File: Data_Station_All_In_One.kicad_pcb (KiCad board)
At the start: 2 copper layers, 97.8 x 76.2 mm, 55 parts, among them J1 Conn_01x02_Male, J10 Conn_01x02_Male, J11 USB_B_Micro, J12 Conn_01x02_Male, J2 Conn_01x02_Male, J3 Conn_01x02_Male, J4 Conn_01x02_Male, J5 Conn_01x02_Male, J6 Conn_01x02_Male, J7 Conn_01x06_Male, J8 Conn_01x06_Male, J9 Conn_01x03_Male, Q1 2N2222, Q2 2N2222, U1 LM7805_TO220, U2 ATMEGA328P-PU, U3 FT232RL, Y1 Crystal

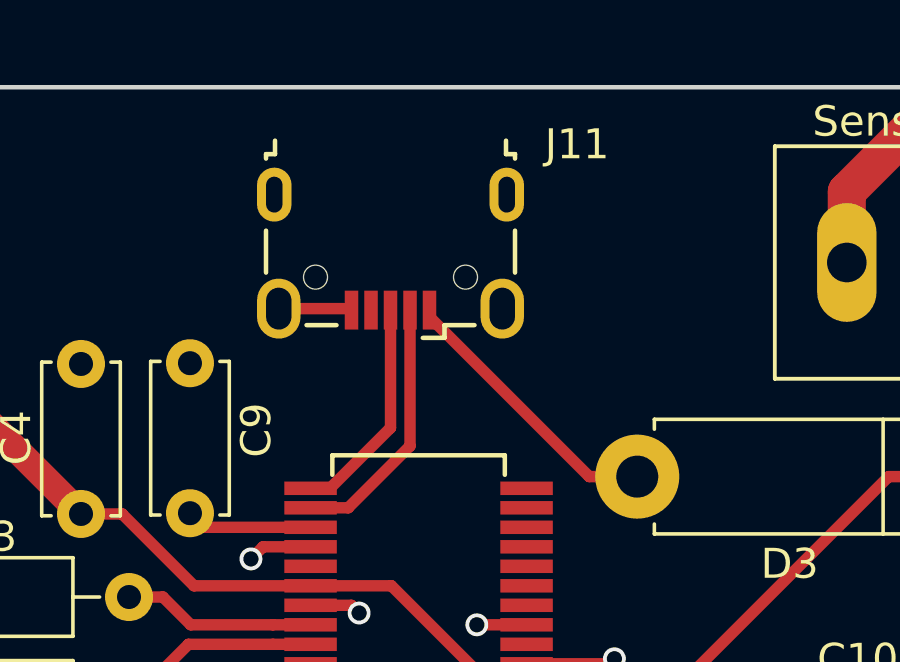
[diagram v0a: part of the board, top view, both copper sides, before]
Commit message: Moved USB Micro to PCB Edge
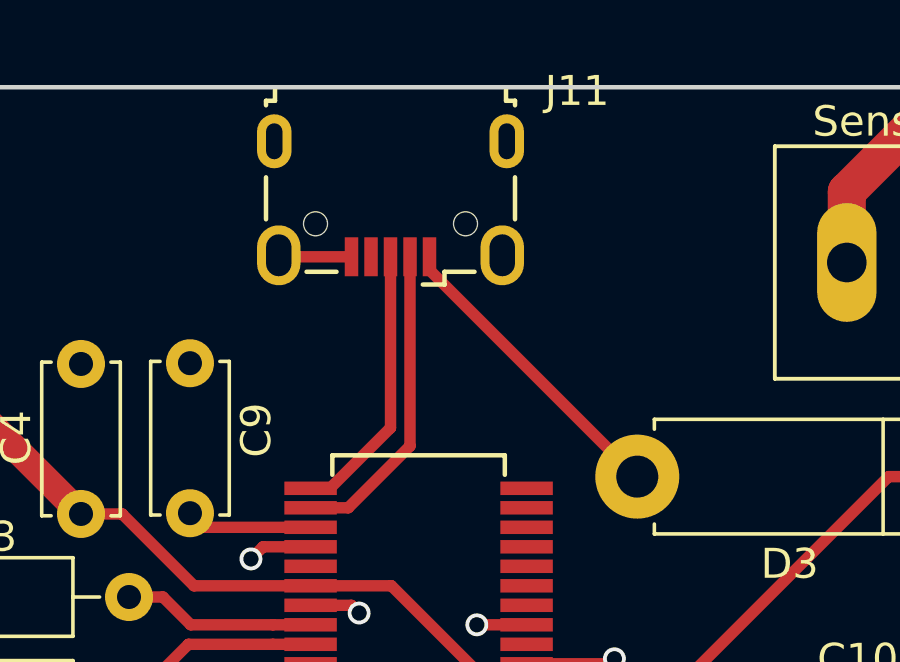
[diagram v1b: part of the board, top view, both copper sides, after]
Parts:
- moved J11 1.78 mm to (126.4, 54.6)
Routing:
- net Net-(J11-Pad3): track 7.42 -> 9.20 mm
- net Net-(J11-Pad2): track 8.70 -> 10.5 mm
- net Net-(D3-Pad2): track 9.36 -> 10.2 mm
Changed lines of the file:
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@@
   )
   (module Connectors_USB:USB_Micro-B_Wuerth-629105150521 (layer F.Cu)
-    (at 126.395 56.3295 180)
+    (at 126.395 54.5515 180)
     (descr "USB Micro-B receptacle, http://www.mouser.com/ds/2/445/629105150521-469306.pdf")
     (tags "usb micro receptacle")
@@
   (segment (start 130.9302 68.7186) (end 129.2722 68.7186) (width 0.381) (layer F.Cu) (net 2) (status 10))
   (via (at 129.2722 68.7186) (size 0.762) (drill 0.508) (layers F.Cu B.Cu) (net 2))
-  (segment (start 125.045 58.1795) (end 125.095 58.2295) (width 0.381) (layer F.Cu) (net 2) (status 30))
-  (segment (start 122.67 58.1795) (end 125.045 58.1795) (width 0.381) (layer F.Cu) (net 2) (status 30))
   (segment (start 181.509 111.786) (end 181.483 111.76) (width 0.381) (layer F.Cu) (net 2) (status 30))
   (segment (start 181.509 115.443) (end 181.509 111.786) (width 0.889) (layer F.Cu) (net 2) (status 30))
@@
   (via (at 125.349 68.326) (size 0.762) (drill 0.508) (layers F.Cu B.Cu) (net 2))
   (segment (start 123.7302 68.0686) (end 125.0916 68.0686) (width 0.381) (layer F.Cu) (net 2) (status 10))
+  (segment (start 122.72 56.4515) (end 122.67 56.4015) (width 0.381) (layer F.Cu) (net 2))
+  (segment (start 125.095 56.4515) (end 122.72 56.4515) (width 0.381) (layer F.Cu) (net 2))
   (segment (start 144.526 98.044) (end 147.066 98.044) (width 1.27) (layer F.Cu) (net 3) (status 20))
   (segment (start 139.446 92.964) (end 144.526 98.044) (width 1.27) (layer F.Cu) (net 3) (status 10))
@@
   (segment (start 188.261 56.642) (end 186.89 56.642) (width 0.762) (layer F.Cu) (net 13) (status 10))
   (segment (start 186.89 56.642) (end 166.624 76.908) (width 0.762) (layer F.Cu) (net 13))
-  (segment (start 193.04 68.58) (end 199.39 68.58) (width 0.381) (layer F.Cu) (net 39) (status 30))
   (segment (start 163.322 81.3435) (end 163.322 80.264) (width 0.381) (layer F.Cu) (net 14) (status 20))
   (segment (start 159.7025 84.963) (end 163.322 81.3435) (width 0.381) (layer F.Cu) (net 14))
@@
   (segment (start 162.052 108.331) (end 163.31037 108.331) (width 0.381) (layer F.Cu) (net 25) (status 10))
   (segment (start 163.31037 108.331) (end 164.45337 109.474) (width 0.381) (layer F.Cu) (net 25))
-  (segment (start 126.395 58.2295) (end 126.395 62.1538) (width 0.381) (layer F.Cu) (net 40) (status 10))
-  (segment (start 124.3802 64.1686) (end 123.7302 64.1686) (width 0.381) (layer F.Cu) (net 40) (status 30))
-  (segment (start 126.395 62.1538) (end 124.3802 64.1686) (width 0.381) (layer F.Cu) (net 40) (status 20))
-  (segment (start 124.9862 64.8186) (end 123.7302 64.8186) (width 0.381) (layer F.Cu) (net 41) (status 20))
-  (segment (start 127.045 58.2295) (end 127.045 62.7598) (width 0.381) (layer F.Cu) (net 41) (status 10))
-  (segment (start 127.045 62.7598) (end 124.9862 64.8186) (width 0.381) (layer F.Cu) (net 41))
   (segment (start 147.066 108.204) (end 151.892 108.204) (width 0.381) (layer F.Cu) (net 26) (status 30))
   (segment (start 151.892 105.156) (end 151.892 108.204) (width 0.381) (layer F.Cu) (net 26) (status 30))
@@
   (segment (start 162.052 105.029) (end 163.449 105.029) (width 0.381) (layer F.Cu) (net 36) (status 10))
   (segment (start 163.449 105.029) (end 164.592 103.886) (width 0.381) (layer F.Cu) (net 36))
-  (segment (start 133.0198 63.7794) (end 134.62 63.7794) (width 0.381) (layer F.Cu) (net 37) (status 20))
-  (segment (start 127.695 58.2295) (end 127.695 58.4546) (width 0.381) (layer F.Cu) (net 37) (status 30))
-  (segment (start 127.695 58.4546) (end 133.0198 63.7794) (width 0.381) (layer F.Cu) (net 37) (status 10))
+  (segment (start 134.5819 63.7794) (end 134.62 63.7794) (width 0.381) (layer F.Cu) (net 37))
+  (segment (start 127.695 56.4515) (end 127.695 56.8925) (width 0.381) (layer F.Cu) (net 37))
+  (segment (start 127.695 56.8925) (end 134.5819 63.7794) (width 0.381) (layer F.Cu) (net 37))
   (segment (start 199.263 76.073) (end 199.39 76.2) (width 0.381) (layer F.Cu) (net 38) (status 30))
   (segment (start 192.405 76.073) (end 199.263 76.073) (width 0.381) (layer F.Cu) (net 38) (status 20))
   (segment (start 185.801 73.533) (end 189.865 73.533) (width 0.381) (layer F.Cu) (net 38) (status 10))
   (segment (start 189.865 73.533) (end 192.405 76.073) (width 0.381) (layer F.Cu) (net 38))
+  (segment (start 193.04 68.58) (end 199.39 68.58) (width 0.381) (layer F.Cu) (net 39) (status 30))
+  (segment (start 124.3802 64.1686) (end 123.7302 64.1686) (width 0.381) (layer F.Cu) (net 40))
+  (segment (start 126.395 56.4515) (end 126.395 62.1538) (width 0.381) (layer F.Cu) (net 40))
+  (segment (start 126.395 62.1538) (end 124.3802 64.1686) (width 0.381) (layer F.Cu) (net 40))
+  (segment (start 124.9862 64.8186) (end 123.7302 64.8186) (width 0.381) (layer F.Cu) (net 41))
+  (segment (start 127.045 56.4515) (end 127.045 62.7598) (width 0.381) (layer F.Cu) (net 41))
+  (segment (start 127.045 62.7598) (end 124.9862 64.8186) (width 0.381) (layer F.Cu) (net 41))
   (segment (start 175.316 118.943) (end 175.26 118.999) (width 0.381) (layer F.Cu) (net 42) (status 30))
   (segment (start 175.26 118.999) (end 169.799 118.999) (width 0.889) (layer F.Cu) (net 42) (status 30))

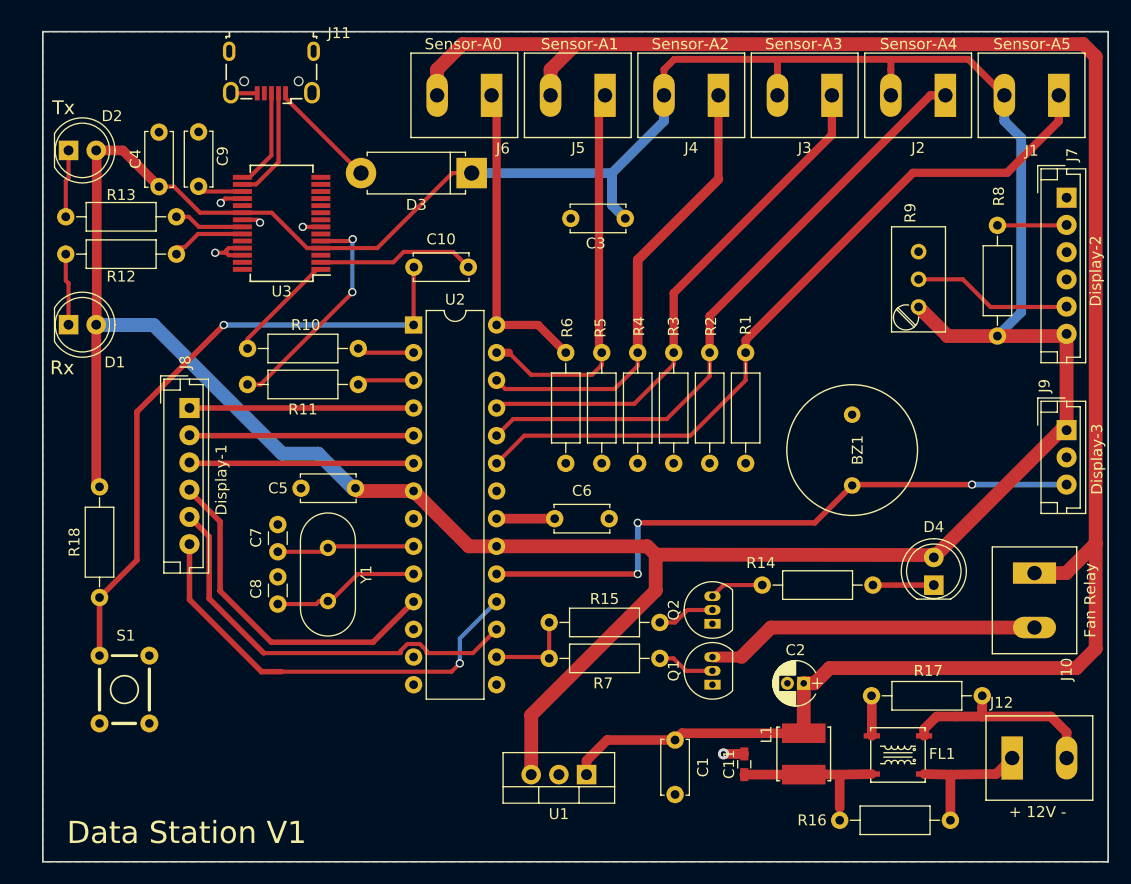
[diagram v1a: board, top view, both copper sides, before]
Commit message: updated to reflect actual order
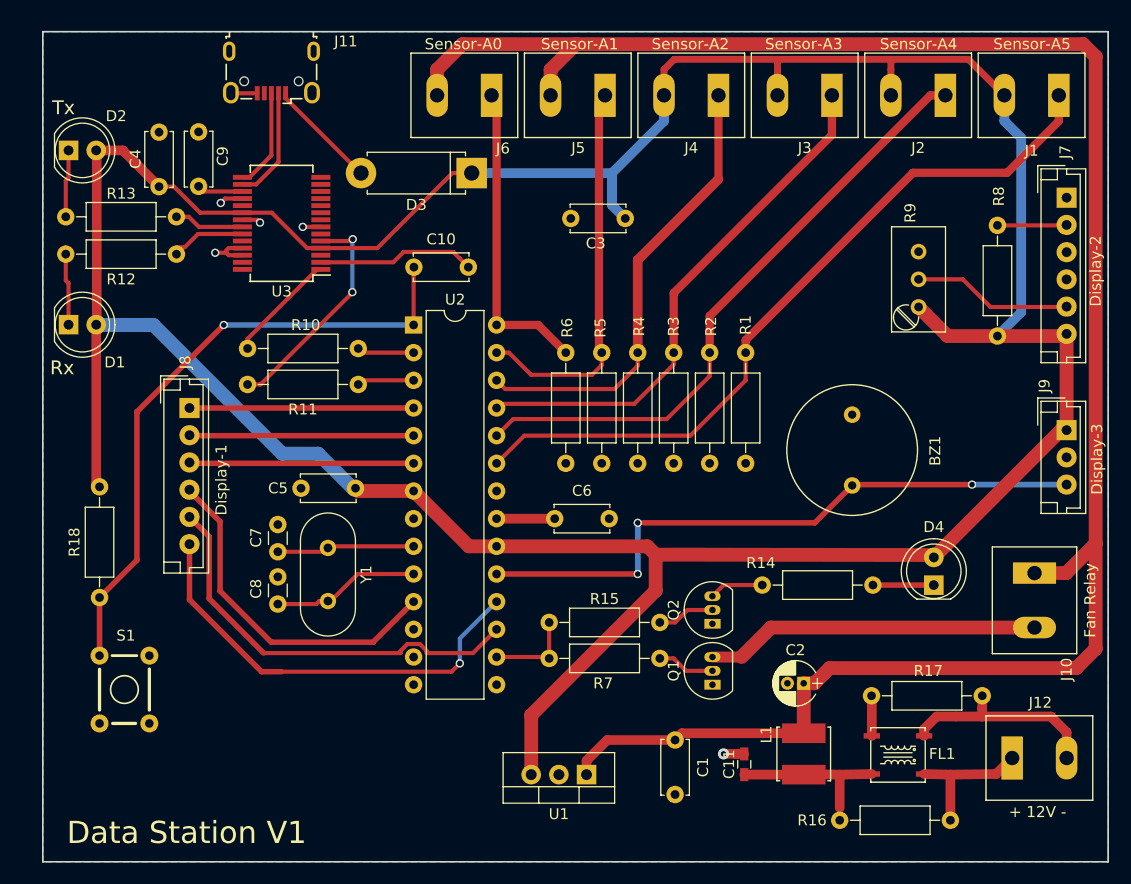
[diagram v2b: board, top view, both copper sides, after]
